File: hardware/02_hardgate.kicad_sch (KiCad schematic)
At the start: 12 parts, among them SW1 TL3340AF160QG, U2 TPS26600PWPR

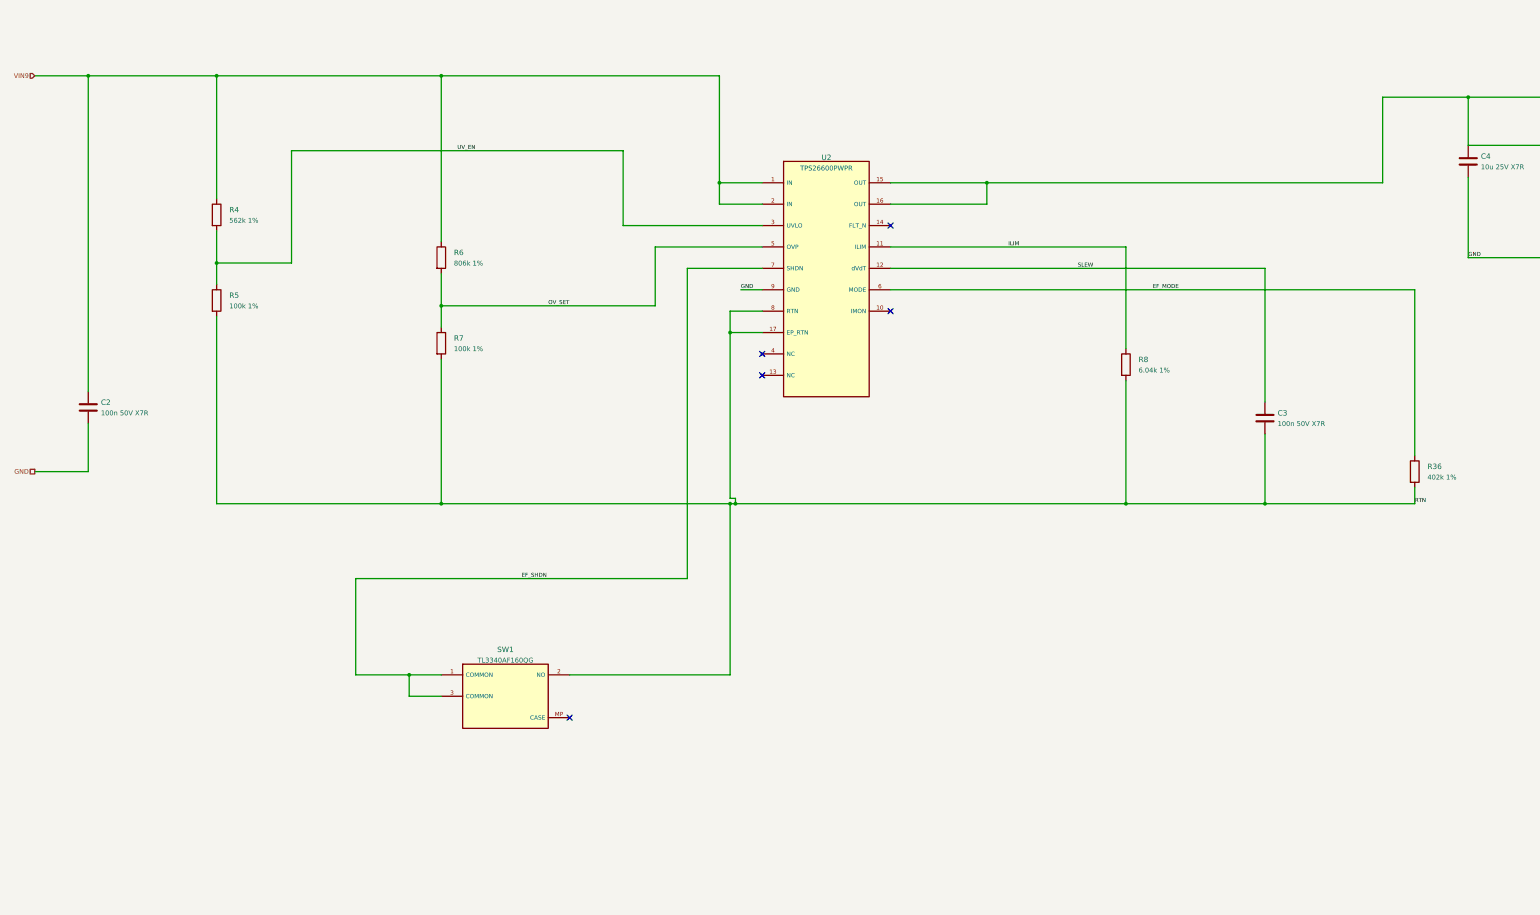
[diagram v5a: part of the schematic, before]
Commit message: Use standard vias and front-only Economy assembly with Basic passive networks and DNP LED
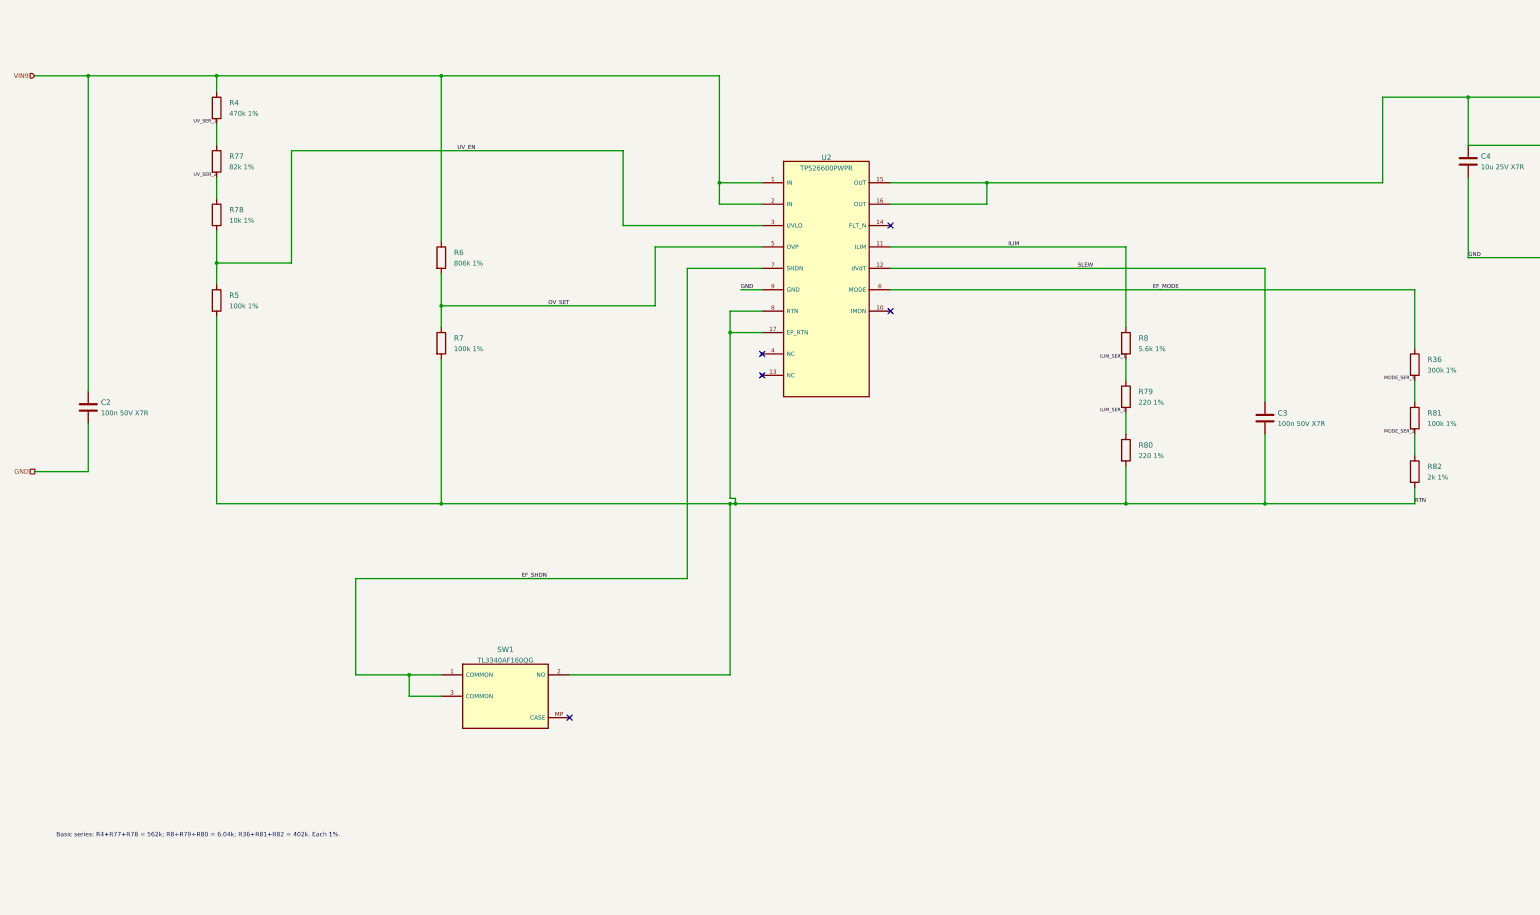
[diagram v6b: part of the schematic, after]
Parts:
- added R77: 82k 1%, BigModular:R_0603_1608Metric, symbol BigModular:Device_R
- added R78: 10k 1%, BigModular:R_0603_1608Metric, symbol BigModular:Device_R
- added R79, R80: 220 1%, BigModular:R_0603_1608Metric, symbol BigModular:Device_R
- added R81: 100k 1%, BigModular:R_0603_1608Metric, symbol BigModular:Device_R
- added R82: 2k 1%, BigModular:R_0603_1608Metric, symbol BigModular:Device_R
- C4: LCSC (none) -> C14860; MPN (none) -> CL31B106KAHNNNE; Manufacturer (none) -> Samsung Electro-Mechanics
- R36: value 402k 1% -> 300k 1%; LCSC C23048 -> C23024; MPN 0603WAF4023T5E -> 0603WAF3003T5E; Manufacturer (none) -> UNI-ROYAL(Uniroyal Elec); NOTE Prototype candidate; qualify ratings, land pattern and oper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 -> Basic/Economy series member: R4+R77+R78=562k; R8+R79+R80=6.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
- R4: value 562k 1% -> 470k 1%; LCSC C23205 -> C23178; MPN 0603WAF5623T5E -> 0603WAF4703T5E; Manufacturer (none) -> UNI-ROYAL(Uniroyal Elec); NOTE Prototype candidate; qualify ratings, land pattern and oper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 -> Basic/Economy series member: R4+R77+R78=562k; R8+R79+R80=6.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
- R8: value 6.04k 1% -> 5.6k 1%; LCSC C25977 -> C23189; MPN 0603WAF6041T5E -> 0603WAF5601T5E; Manufacturer (none) -> UNI-ROYAL(Uniroyal Elec); NOTE Prototype candidate; qualify ratings, land pattern and oper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 -> Basic/Economy series member: R4+R77+R78=562k; R8+R79+R80=6.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
- SW1: JLCPCB Audit Requirements {"assembly": "manual", "reason": "User-selected manual inte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 -> {"assembly": "jlcpcb", "reason": "Economy catalog candidate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; JLCPCB Exclude yes -> no; LCSC (none) -> C2886925; Manufacturer (none) -> E-Switch; NOTE P021301 Rev B contacts1+3 common; contact2 RTN. Press disables eFuse; release retries latch-off subject to UV/OV. Internal SHDN pullup only; no downstream EN or external supply load. Case MP floating. -> P021301 Rev B contacts1+3 common; contact2 RTN. Press disables eFuse; release retries latch-off subject to UV/OV. Internal SHDN pullup only; no downstream EN or external supply load. Case MP floating. Extended/Economy catalog candidate; SMT J-leads/case paste retained. No supplier process/quote approval.
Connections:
- net RTN: now also R80.2, R82.2; no longer R36.2, R8.2
- net UV_EN: now also R78.2; no longer R4.2
- new net ILIM_SER_1: R79.1, R8.2
- new net ILIM_SER_2: R79.2, R80.1
- new net MODE_SER_1: R36.2, R81.1
- new net MODE_SER_2: R81.2, R82.1
- new net UV_SER_1: R4.2, R77.1
- new net UV_SER_2: R77.2, R78.1
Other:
- note added: "Basic series: R4+R77+R78 = 562k; R8+R79+R80 = 6.04k; R36+R81+R82 = 402k. Each 1%."
- moved on the sheet: R36, R4, R8

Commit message: Apply Basic passive substitutions with corrected dividers, 1206 capacitor routing and verified prototype release
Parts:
- C4: value 10u 25V X7R -> 10u 50V X5R; LCSC C14860 -> C13585; MPN CL31B106KAHNNNE -> CL31A106KBHNNNE
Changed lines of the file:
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@@
 		)
 	)
-	(symbol (lib_id "BigModular:Device_C") (at 365.76 78.74 0) (unit 1) (body_style 1) (exclude_from_sim no) (in_bom yes) (on_board yes) (in_pos_files yes) (dnp no) (property "Reference" "C4" (at 368.76 77.54 0) (show_name no) (do_not_autoplace no) (effects (font (size 1.27 1.27)) (justify left))) (property "Value" "10u 25V X7R" (at 368.76 80.08 0) (show_name no) (do_not_autoplace no) (effects (font (size 1.15 1.15)) (justify left))) (property "Footprint" "BigModular:C_1206_3216Metric" (at 365.76 78.74 0) (hide yes) (show_name no) (do_not_autoplace no) (effects (font (size 1 1)))) (property "Datasheet" "https://www.lcsc.com/datasheet/lcsc_datasheet_2304140030_Samsung-Electro-Mechanics-CL31B106KAHNNNE_C14860.pdf" (at 365.76 78.74 0) (hide yes) (show_name no) (do_not_autoplace no) (effects (font (size 1 1)))) (property "Description" "" (at 365.76 78.74 0) (show_name no) (do_not_autoplace no) (effects (font (size 1.27 1.27)))) (property "MPN" "CL31B106KAHNNNE" (at 365.76 78.74 0) (hide yes) (show_name no) (do_not_autoplace no) (effects (font (size 1 1)))) (property "LCSC" "C14860" (at 365.76 78.74 0) (hide yes) (show_name no) (do_not_autoplace no) (effects (font (size 1 1)))) (property "NOTE" "Effective capacitance under DC bias and temperature must be verified; no automatic reuse approval." (at 365.76 78.74 0) (hide yes) (show_name no) (do_not_autoplace no) (effects (font (size 1 1)))) (property "JLCPCB Exclude" "no" (at 365.76 78.74 0) (hide yes) (show_name no) (do_not_autoplace no) (effects (font (size 1 1)))) (property "JLCPCB Audit Requirements" "{}" (at 365.76 78.74 0) (hide yes) (show_name no) (do_not_autoplace no) (effects (font (size 1 1)))) (pin "1") (pin "2") (instances (project "big_modular" (path "/d567704c-57ad-5df1-b183-cadb01fd8972/a1db43c9-8f66-506b-99cb-e15d2f492e56" (reference "C4") (unit 1)))) (property "Manufacturer" "Samsung Electro-Mechanics" (at 368.76 80.08 0) (show_name no) (do_not_autoplace no) (effects (font (size 1.15 1.15)) (justify left) hide)))
+	(symbol (lib_id "BigModular:Device_C") (at 365.76 78.74 0) (unit 1) (body_style 1) (exclude_from_sim no) (in_bom yes) (on_board yes) (in_pos_files yes) (dnp no) (property "Reference" "C4" (at 368.76 77.54 0) (show_name no) (do_not_autoplace no) (effects (font (size 1.27 1.27)) (justify left))) (property "Value" "10u 50V X5R" (at 368.76 80.08 0) (show_name no) (do_not_autoplace no) (effects (font (size 1.15 1.15)) (justify left))) (property "Footprint" "BigModular:C_1206_3216Metric" (at 365.76 78.74 0) (hide yes) (show_name no) (do_not_autoplace no) (effects (font (size 1 1)))) (property "Datasheet" "https://www.lcsc.com/datasheet/lcsc_datasheet_2304140030_Samsung-Electro-Mechanics-CL31A106KBHNNNE_C13585.pdf" (at 365.76 78.74 0) (hide yes) (show_name no) (do_not_autoplace no) (effects (font (size 1 1)))) (property "Description" "" (at 365.76 78.74 0) (show_name no) (do_not_autoplace no) (effects (font (size 1.27 1.27)))) (property "MPN" "CL31A106KBHNNNE" (at 365.76 78.74 0) (hide yes) (show_name no) (do_not_autoplace no) (effects (font (size 1 1)))) (property "LCSC" "C13585" (at 365.76 78.74 0) (hide yes) (show_name no) (do_not_autoplace no) (effects (font (size 1 1)))) (property "NOTE" "Effective capacitance under DC bias and temperature must be verified; no automatic reuse approval." (at 365.76 78.74 0) (hide yes) (show_name no) (do_not_autoplace no) (effects (font (size 1 1)))) (property "JLCPCB Exclude" "no" (at 365.76 78.74 0) (hide yes) (show_name no) (do_not_autoplace no) (effects (font (size 1 1)))) (property "JLCPCB Audit Requirements" "{}" (at 365.76 78.74 0) (hide yes) (show_name no) (do_not_autoplace no) (effects (font (size 1 1)))) (pin "1") (pin "2") (instances (project "big_modular" (path "/d567704c-57ad-5df1-b183-cadb01fd8972/a1db43c9-8f66-506b-99cb-e15d2f492e56" (reference "C4") (unit 1)))) (property "Manufacturer" "Samsung Electro-Mechanics" (at 368.76 80.08 0) (show_name no) (do_not_autoplace no) (effects (font (size 1.15 1.15)) (justify left) hide)))
 	(symbol (lib_id "BigModular:TL3340AF160QG") (at 137.16 205.74 0) (unit 1) (body_style 1) (exclude_from_sim no) (in_bom yes) (on_board yes) (in_pos_files yes) (dnp no) (property "Reference" "SW1" (at 137.16 194.66 0) (show_name no) (do_not_autoplace no) (effects (font (size 1.27 1.27)))) (property "Value" "TL3340AF160QG" (at 137.16 197.2 0) (show_name no) (do_not_autoplace no) (effects (font (size 1.15 1.15)))) (property "Footprint" "BigModular:SW_TL3340AF160QG_HandSolder" (at 137.16 205.74 0) (hide yes) (show_name no) (do_not_autoplace no) (effects (font (size 1 1)))) (property "Datasheet" "https://configured-product-images.s3.amazonaws.com/2D/specs/TL3340AF160QG.pdf" (at 137.16 205.74 0) (hide yes) (show_name no) (do_not_autoplace no) (effects (font (size 1 1)))) (property "Description" "" (at 137.16 205.74 0) (show_name no) (do_not_autoplace no) (effects (font (size 1.27 1.27)))) (property "MPN" "TL3340AF160QG" (at 137.16 205.74 0) (hide yes) (show_name no) (do_not_autoplace no) (effects (font (size 1 1)))) (property "LCSC" "C2886925" (at 137.16 205.74 0) (hide yes) (show_name no) (do_not_autoplace no) (effects (font (size 1 1)))) (property "NOTE" "P021301 Rev B contacts1+3 common; contact2 RTN. Press disables eFuse; release retries latch-off subject to UV/OV. Internal SHDN pullup only; no downstream EN or external supply load. Case MP floating. Extended/Economy catalog candidate; SMT J-leads/case paste retained. No supplier process/quote approval." (at 137.16 205.74 0) (hide yes) (show_name no) (do_not_autoplace no) (effects (font (size 1 1)))) (property "JLCPCB Exclude" "no" (at 137.16 205.74 0) (hide yes) (show_name no) (do_not_autoplace no) (effects (font (size 1 1)))) (property "JLCPCB Audit Requirements" "{\"assembly\": \"jlcpcb\", \"reason\": \"Economy catalog candidate; supplier process/preview approval pending.\"}" (at 137.16 205.74 0) (hide yes) (show_name no) (do_not_autoplace no) (effects (font (size 1 1)))) (pin "1") (pin "3") (pin "2") (pin "MP") (instances (project "big_modular" (path "/d567704c-57ad-5df1-b183-cadb01fd8972/a1db43c9-8f66-506b-99cb-e15d2f492e56" (reference "SW1") (unit 1)))) (property "Manufacturer" "E-Switch" (at 137.16 197.2 0) (show_name no) (do_not_autoplace no) (effects (font (size 1.15 1.15)) hide)))
 	(symbol (lib_id "BigModular:Device_R") (at 353.06 127 0) (unit 1) (body_style 1) (exclude_from_sim no) (in_bom yes) (on_board yes) (in_pos_files yes) (dnp no) (property "Reference" "R36" (at 356.06 125.8 0) (show_name no) (do_not_autoplace no) (effects (font (size 1.27 1.27)) (justify left))) (property "Value" "300k 1%" (at 356.06 128.34 0) (show_name no) (do_not_autoplace no) (effects (font (size 1.15 1.15)) (justify left))) (property "Footprint" "BigModular:R_0603_1608Metric" (at 353.06 127 0) (hide yes) (show_name no) (do_not_autoplace no) (effects (font (size 1 1)))) (property "Datasheet" "https://www.lcsc.com/datasheet/lcsc_datasheet_2206010116_UNI-ROYAL-Uniroyal-Elec-0603WAF3003T5E_C23024.pdf" (at 353.06 127 0) (hide yes) (show_name no) (do_not_autoplace no) (effects (font (size 1 1)))) (property "Description" "" (at 353.06 127 0) (show_name no) (do_not_autoplace no) (effects (font (size 1.27 1.27)))) (property "MPN" "0603WAF3003T5E" (at 353.06 127 0) (hide yes) (show_name no) (do_not_autoplace no) (effects (font (size 1 1)))) (property "LCSC" "C23024" (at 353.06 127 0) (hide yes) (show_name no) (do_not_autoplace no) (effects (font (size 1 1)))) (property "NOTE" "Basic/Economy series member: R4+R77+R78=562k; R8+R79+R80=6.04k; R36+R81+R82=402k. Each 1%, 100ppm/K, 100mW/75V. See basic-passives-disposition.md for independent corners, fault/derating and local RTN review." (at 353.06 127 0) (hide yes) (show_name no) (do_not_autoplace no) (effects (font (size 1 1)))) (property "JLCPCB Exclude" "no" (at 353.06 127 0) (hide yes) (show_name no) (do_not_autoplace no) (effects (font (size 1 1)))) (property "JLCPCB Audit Requirements" "{}" (at 353.06 127 0) (hide yes) (show_name no) (do_not_autoplace no) (effects (font (size 1 1)))) (pin "1") (pin "2") (instances (project "big_modular" (path "/d567704c-57ad-5df1-b183-cadb01fd8972/a1db43c9-8f66-506b-99cb-e15d2f492e56" (reference "R36") (unit 1)))) (property "Manufacturer" "UNI-ROYAL(Uniroyal Elec)" (at 356.06 128.34 0) (show_name no) (do_not_autoplace no) (effects (font (size 1.15 1.15)) (justify left) hide)))
